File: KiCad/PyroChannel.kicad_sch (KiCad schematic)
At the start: 5 parts, among them Q1 IRLML0030

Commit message: very rough sketch layout
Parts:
- renumbered R2 to R10, R3 to R7, R4 to R8, R1 to R9
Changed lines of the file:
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@@
 		(dnp no)
 		(fields_autoplaced yes)
-		(property "Reference" "#PWR03"
+		(property "Reference" "#PWR040"
 			(at 157.48 107.95 0)
 			(effects
@@
 			(project ""
 				(path "/16f8cce7-467e-4342-b55a-00af81cd6f69/fc7ffde7-f19b-4eb6-b923-3f87c2b4142b"
-					(reference "#PWR03")
+					(reference "#PWR040")
 					(unit 1)
 				)
@@
 		(dnp no)
 		(fields_autoplaced yes)
-		(property "Reference" "#PWR02"
+		(property "Reference" "#PWR039"
 			(at 147.32 107.95 0)
 			(effects
@@
 			(project ""
 				(path "/16f8cce7-467e-4342-b55a-00af81cd6f69/fc7ffde7-f19b-4eb6-b923-3f87c2b4142b"
-					(reference "#PWR02")
+					(reference "#PWR039")
 					(unit 1)
 				)
@@
 		(dnp no)
 		(fields_autoplaced yes)
-		(property "Reference" "R1"
+		(property "Reference" "R9"
 			(at 160.02 81.2799 0)
 			(effects
@@
 			(project ""
 				(path "/16f8cce7-467e-4342-b55a-00af81cd6f69/fc7ffde7-f19b-4eb6-b923-3f87c2b4142b"
-					(reference "R1")
+					(reference "R9")
 					(unit 1)
 				)
@@
 		(dnp no)
 		(fields_autoplaced yes)
-		(property "Reference" "#PWR01"
+		(property "Reference" "#PWR038"
 			(at 138.43 115.57 0)
 			(effects
@@
 			(project ""
 				(path "/16f8cce7-467e-4342-b55a-00af81cd6f69/fc7ffde7-f19b-4eb6-b923-3f87c2b4142b"
-					(reference "#PWR01")
+					(reference "#PWR038")
 					(unit 1)
 				)
@@
 		(dnp no)
 		(fields_autoplaced yes)
-		(property "Reference" "R3"
+		(property "Reference" "R7"
 			(at 129.54 87.63 90)
 			(effects
@@
 			(project ""
 				(path "/16f8cce7-467e-4342-b55a-00af81cd6f69/fc7ffde7-f19b-4eb6-b923-3f87c2b4142b"
-					(reference "R3")
+					(reference "R7")
 					(unit 1)
 				)
@@
 		(dnp no)
 		(fields_autoplaced yes)
-		(property "Reference" "R4"
+		(property "Reference" "R8"
 			(at 140.97 104.1399 0)
 			(effects
@@
 			(project ""
 				(path "/16f8cce7-467e-4342-b55a-00af81cd6f69/fc7ffde7-f19b-4eb6-b923-3f87c2b4142b"
-					(reference "R4")
+					(reference "R8")
 					(unit 1)
 				)
@@
 		(dnp no)
 		(fields_autoplaced yes)
-		(property "Reference" "R2"
+		(property "Reference" "R10"
 			(at 160.02 95.2499 0)
 			(effects
@@
 			(project ""
 				(path "/16f8cce7-467e-4342-b55a-00af81cd6f69/fc7ffde7-f19b-4eb6-b923-3f87c2b4142b"
-					(reference "R2")
-					(unit 1)
-				)
+					(reference "R10")
+					(unit 1)
+				)

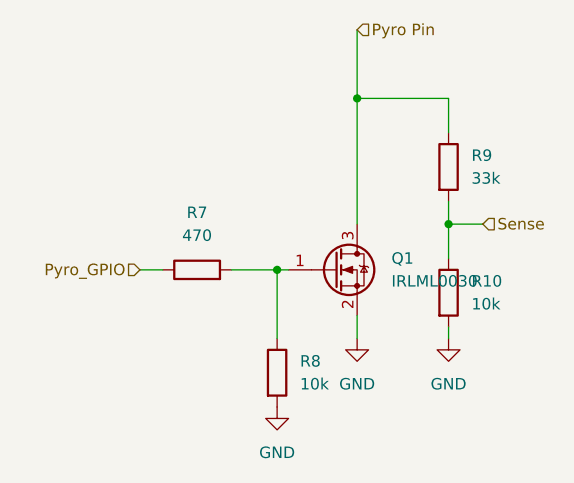
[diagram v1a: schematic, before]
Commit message: Added Pyrochannels
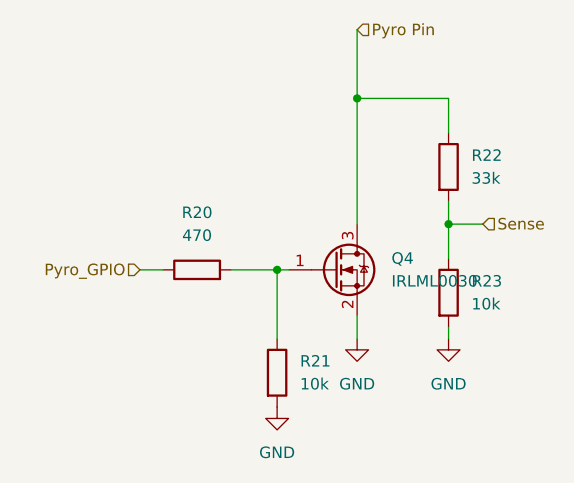
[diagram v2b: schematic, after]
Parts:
- renumbered Q1 to Q4, R7 to R20, R8 to R21, R9 to R22, R10 to R23
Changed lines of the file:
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@@
 		(dnp no)
 		(fields_autoplaced yes)
-		(property "Reference" "#PWR040"
+		(property "Reference" "#PWR072"
 			(at 157.48 107.95 0)
 			(effects
@@
 		)
 		(instances
-			(project ""
-				(path "/16f8cce7-467e-4342-b55a-00af81cd6f69/fc7ffde7-f19b-4eb6-b923-3f87c2b4142b"
-					(reference "#PWR040")
-					(unit 1)
-				)
-			)
-			(project ""
-				(path "/4b87987a-7eb1-4c92-aab7-f7fab4804919"
-					(reference "#PWR03")
+			(project "Senior Project"
+				(path "/16f8cce7-467e-4342-b55a-00af81cd6f69/4f56c78f-4532-4c9f-be6c-2bbf693c5fca"
+					(reference "#PWR072")
+					(unit 1)
+				)
+				(path "/16f8cce7-467e-4342-b55a-00af81cd6f69/528e247e-1625-48b4-9899-73b4b85367ce"
+					(reference "#PWR069")
+					(unit 1)
+				)
+				(path "/16f8cce7-467e-4342-b55a-00af81cd6f69/553e2c15-6dd9-455d-b91b-1c20c70d481b"
+					(reference "#PWR066")
 					(unit 1)
 				)
@@
 		(dnp no)
 		(fields_autoplaced yes)
-		(property "Reference" "#PWR039"
+		(property "Reference" "#PWR071"
 			(at 147.32 107.95 0)
 			(effects
@@
 		)
 		(instances
-			(project ""
-				(path "/16f8cce7-467e-4342-b55a-00af81cd6f69/fc7ffde7-f19b-4eb6-b923-3f87c2b4142b"
-					(reference "#PWR039")
-					(unit 1)
-				)
-			)
-			(project ""
-				(path "/4b87987a-7eb1-4c92-aab7-f7fab4804919"
-					(reference "#PWR02")
+			(project "Senior Project"
+				(path "/16f8cce7-467e-4342-b55a-00af81cd6f69/4f56c78f-4532-4c9f-be6c-2bbf693c5fca"
+					(reference "#PWR071")
+					(unit 1)
+				)
+				(path "/16f8cce7-467e-4342-b55a-00af81cd6f69/528e247e-1625-48b4-9899-73b4b85367ce"
+					(reference "#PWR068")
+					(unit 1)
+				)
+				(path "/16f8cce7-467e-4342-b55a-00af81cd6f69/553e2c15-6dd9-455d-b91b-1c20c70d481b"
+					(reference "#PWR057")
 					(unit 1)
 				)
@@
 		(dnp no)
 		(fields_autoplaced yes)
-		(property "Reference" "R9"
+		(property "Reference" "R22"
 			(at 160.02 81.2799 0)
 			(effects
@@
 		)
 		(instances
-			(project ""
-				(path "/16f8cce7-467e-4342-b55a-00af81cd6f69/fc7ffde7-f19b-4eb6-b923-3f87c2b4142b"
-					(reference "R9")
-					(unit 1)
-				)
-			)
-			(project ""
-				(path "/4b87987a-7eb1-4c92-aab7-f7fab4804919"
-					(reference "R1")
+			(project "Senior Project"
+				(path "/16f8cce7-467e-4342-b55a-00af81cd6f69/4f56c78f-4532-4c9f-be6c-2bbf693c5fca"
+					(reference "R22")
+					(unit 1)
+				)
+				(path "/16f8cce7-467e-4342-b55a-00af81cd6f69/528e247e-1625-48b4-9899-73b4b85367ce"
+					(reference "R18")
+					(unit 1)
+				)
+				(path "/16f8cce7-467e-4342-b55a-00af81cd6f69/553e2c15-6dd9-455d-b91b-1c20c70d481b"
+					(reference "R14")
 					(unit 1)
 				)
@@
 		(dnp no)
 		(fields_autoplaced yes)
-		(property "Reference" "#PWR038"
+		(property "Reference" "#PWR070"
 			(at 138.43 115.57 0)
 			(effects
@@
 		)
 		(instances
-			(project ""
-				(path "/16f8cce7-467e-4342-b55a-00af81cd6f69/fc7ffde7-f19b-4eb6-b923-3f87c2b4142b"
-					(reference "#PWR038")
-					(unit 1)
-				)
-			)
-			(project ""
-				(path "/4b87987a-7eb1-4c92-aab7-f7fab4804919"
-					(reference "#PWR01")
+			(project "Senior Project"
+				(path "/16f8cce7-467e-4342-b55a-00af81cd6f69/4f56c78f-4532-4c9f-be6c-2bbf693c5fca"
+					(reference "#PWR070")
+					(unit 1)
+				)
+				(path "/16f8cce7-467e-4342-b55a-00af81cd6f69/528e247e-1625-48b4-9899-73b4b85367ce"
+					(reference "#PWR067")
+					(unit 1)
+				)
+				(path "/16f8cce7-467e-4342-b55a-00af81cd6f69/553e2c15-6dd9-455d-b91b-1c20c70d481b"
+					(reference "#PWR056")
 					(unit 1)
 				)
@@
 		(dnp no)
 		(fields_autoplaced yes)
-		(property "Reference" "R7"
+		(property "Reference" "R20"
 			(at 129.54 87.63 90)
 			(effects
@@
 		)
 		(instances
-			(project ""
-				(path "/16f8cce7-467e-4342-b55a-00af81cd6f69/fc7ffde7-f19b-4eb6-b923-3f87c2b4142b"
-					(reference "R7")
-					(unit 1)
-				)
-			)
-			(project ""
-				(path "/4b87987a-7eb1-4c92-aab7-f7fab4804919"
-					(reference "R3")
+			(project "Senior Project"
+				(path "/16f8cce7-467e-4342-b55a-00af81cd6f69/4f56c78f-4532-4c9f-be6c-2bbf693c5fca"
+					(reference "R20")
+					(unit 1)
+				)
+				(path "/16f8cce7-467e-4342-b55a-00af81cd6f69/528e247e-1625-48b4-9899-73b4b85367ce"
+					(reference "R16")
+					(unit 1)
+				)
+				(path "/16f8cce7-467e-4342-b55a-00af81cd6f69/553e2c15-6dd9-455d-b91b-1c20c70d481b"
+					(reference "R12")
 					(unit 1)
 				)
@@
 		(dnp no)
 		(fields_autoplaced yes)
-		(property "Reference" "Q1"
+		(property "Reference" "Q4"
 			(at 151.13 92.7099 0)
 			(effects
@@
 		)
 		(instances
-			(project ""
-				(path "/16f8cce7-467e-4342-b55a-00af81cd6f69/fc7ffde7-f19b-4eb6-b923-3f87c2b4142b"
-					(reference "Q1")
-					(unit 1)
-				)
-			)
-			(project ""
-				(path "/4b87987a-7eb1-4c92-aab7-f7fab4804919"
-					(reference "Q1")
+			(project "Senior Project"
+				(path "/16f8cce7-467e-4342-b55a-00af81cd6f69/4f56c78f-4532-4c9f-be6c-2bbf693c5fca"
+					(reference "Q4")
+					(unit 1)
+				)
+				(path "/16f8cce7-467e-4342-b55a-00af81cd6f69/528e247e-1625-48b4-9899-73b4b85367ce"
+					(reference "Q3")
+					(unit 1)
+				)
+				(path "/16f8cce7-467e-4342-b55a-00af81cd6f69/553e2c15-6dd9-455d-b91b-1c20c70d481b"
+					(reference "Q2")
 					(unit 1)
 				)
@@
 		(dnp no)
 		(fields_autoplaced yes)
-		(property "Reference" "R8"
+		(property "Reference" "R21"
 			(at 140.97 104.1399 0)
 			(effects
@@
 		)
 		(instances
-			(project ""
-				(path "/16f8cce7-467e-4342-b55a-00af81cd6f69/fc7ffde7-f19b-4eb6-b923-3f87c2b4142b"
-					(reference "R8")
-					(unit 1)
-				)
-			)
-			(project ""
-				(path "/4b87987a-7eb1-4c92-aab7-f7fab4804919"
-					(reference "R4")
+			(project "Senior Project"
+				(path "/16f8cce7-467e-4342-b55a-00af81cd6f69/4f56c78f-4532-4c9f-be6c-2bbf693c5fca"
+					(reference "R21")
+					(unit 1)
+				)
+				(path "/16f8cce7-467e-4342-b55a-00af81cd6f69/528e247e-1625-48b4-9899-73b4b85367ce"
+					(reference "R17")
+					(unit 1)
+				)
+				(path "/16f8cce7-467e-4342-b55a-00af81cd6f69/553e2c15-6dd9-455d-b91b-1c20c70d481b"
+					(reference "R13")
 					(unit 1)
 				)
@@
 		(dnp no)
 		(fields_autoplaced yes)
-		(property "Reference" "R10"
+		(property "Reference" "R23"
 			(at 160.02 95.2499 0)
 			(effects
@@
 		)
 		(instances
-			(project ""
-				(path "/16f8cce7-467e-4342-b55a-00af81cd6f69/fc7ffde7-f19b-4eb6-b923-3f87c2b4142b"
-					(reference "R10")
-					(unit 1)
-				)
-			)
-			(project ""
-				(path "/4b87987a-7eb1-4c92-aab7-f7fab4804919"
-					(reference "R2")
-					(unit 1)
-				)
+			(project "Senior Project"
+				(path "/16f8cce7-467e-4342-b55a-00af81cd6f69/4f56c78f-4532-4c9f-be6c-2bbf693c5fca"
+					(reference "R23")
+					(unit 1)
+				)
+				(path "/16f8cce7-467e-4342-b55a-00af81cd6f69/528e247e-1625-48b4-9899-73b4b85367ce"
+					(reference "R19")
+					(unit 1)
+				)
+				(path "/16f8cce7-467e-4342-b55a-00af81cd6f69/553e2c15-6dd9-455d-b91b-1c20c70d481b"
+					(reference "R15")
+					(unit 1)
+				)

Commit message: Layout started
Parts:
- renumbered Q4 to Q3, R20 to R16, R21 to R17, R22 to R18, R23 to R19
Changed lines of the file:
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@@
 		(dnp no)
 		(fields_autoplaced yes)
-		(property "Reference" "#PWR072"
+		(property "Reference" "#PWR069"
 			(at 157.48 107.95 0)
 			(effects
@@
 		(instances
 			(project "Senior Project"
-				(path "/16f8cce7-467e-4342-b55a-00af81cd6f69/4f56c78f-4532-4c9f-be6c-2bbf693c5fca"
+				(path "/16f8cce7-467e-4342-b55a-00af81cd6f69/553e2c15-6dd9-455d-b91b-1c20c70d481b"
+					(reference "#PWR066")
+					(unit 1)
+				)
+				(path "/16f8cce7-467e-4342-b55a-00af81cd6f69/60268ff6-e480-4c50-9139-8340585ef982"
+					(reference "#PWR069")
+					(unit 1)
+				)
+				(path "/16f8cce7-467e-4342-b55a-00af81cd6f69/93da445a-87ee-42db-a7a9-6194d5b9218b"
 					(reference "#PWR072")
-					(unit 1)
-				)
-				(path "/16f8cce7-467e-4342-b55a-00af81cd6f69/528e247e-1625-48b4-9899-73b4b85367ce"
-					(reference "#PWR069")
-					(unit 1)
-				)
-				(path "/16f8cce7-467e-4342-b55a-00af81cd6f69/553e2c15-6dd9-455d-b91b-1c20c70d481b"
-					(reference "#PWR066")
 					(unit 1)
 				)
@@
 		(dnp no)
 		(fields_autoplaced yes)
-		(property "Reference" "#PWR071"
+		(property "Reference" "#PWR068"
 			(at 147.32 107.95 0)
 			(effects
@@
 		(instances
 			(project "Senior Project"
-				(path "/16f8cce7-467e-4342-b55a-00af81cd6f69/4f56c78f-4532-4c9f-be6c-2bbf693c5fca"
+				(path "/16f8cce7-467e-4342-b55a-00af81cd6f69/553e2c15-6dd9-455d-b91b-1c20c70d481b"
+					(reference "#PWR057")
+					(unit 1)
+				)
+				(path "/16f8cce7-467e-4342-b55a-00af81cd6f69/60268ff6-e480-4c50-9139-8340585ef982"
+					(reference "#PWR068")
+					(unit 1)
+				)
+				(path "/16f8cce7-467e-4342-b55a-00af81cd6f69/93da445a-87ee-42db-a7a9-6194d5b9218b"
 					(reference "#PWR071")
-					(unit 1)
-				)
-				(path "/16f8cce7-467e-4342-b55a-00af81cd6f69/528e247e-1625-48b4-9899-73b4b85367ce"
-					(reference "#PWR068")
-					(unit 1)
-				)
-				(path "/16f8cce7-467e-4342-b55a-00af81cd6f69/553e2c15-6dd9-455d-b91b-1c20c70d481b"
-					(reference "#PWR057")
 					(unit 1)
 				)
@@
 		(dnp no)
 		(fields_autoplaced yes)
-		(property "Reference" "R22"
+		(property "Reference" "R18"
 			(at 160.02 81.2799 0)
 			(effects
@@
 		(instances
 			(project "Senior Project"
-				(path "/16f8cce7-467e-4342-b55a-00af81cd6f69/4f56c78f-4532-4c9f-be6c-2bbf693c5fca"
+				(path "/16f8cce7-467e-4342-b55a-00af81cd6f69/553e2c15-6dd9-455d-b91b-1c20c70d481b"
+					(reference "R14")
+					(unit 1)
+				)
+				(path "/16f8cce7-467e-4342-b55a-00af81cd6f69/60268ff6-e480-4c50-9139-8340585ef982"
+					(reference "R18")
+					(unit 1)
+				)
+				(path "/16f8cce7-467e-4342-b55a-00af81cd6f69/93da445a-87ee-42db-a7a9-6194d5b9218b"
 					(reference "R22")
-					(unit 1)
-				)
-				(path "/16f8cce7-467e-4342-b55a-00af81cd6f69/528e247e-1625-48b4-9899-73b4b85367ce"
-					(reference "R18")
-					(unit 1)
-				)
-				(path "/16f8cce7-467e-4342-b55a-00af81cd6f69/553e2c15-6dd9-455d-b91b-1c20c70d481b"
-					(reference "R14")
 					(unit 1)
 				)
@@
 		(dnp no)
 		(fields_autoplaced yes)
-		(property "Reference" "#PWR070"
+		(property "Reference" "#PWR067"
 			(at 138.43 115.57 0)
 			(effects
@@
 		(instances
 			(project "Senior Project"
-				(path "/16f8cce7-467e-4342-b55a-00af81cd6f69/4f56c78f-4532-4c9f-be6c-2bbf693c5fca"
+				(path "/16f8cce7-467e-4342-b55a-00af81cd6f69/553e2c15-6dd9-455d-b91b-1c20c70d481b"
+					(reference "#PWR056")
+					(unit 1)
+				)
+				(path "/16f8cce7-467e-4342-b55a-00af81cd6f69/60268ff6-e480-4c50-9139-8340585ef982"
+					(reference "#PWR067")
+					(unit 1)
+				)
+				(path "/16f8cce7-467e-4342-b55a-00af81cd6f69/93da445a-87ee-42db-a7a9-6194d5b9218b"
 					(reference "#PWR070")
-					(unit 1)
-				)
-				(path "/16f8cce7-467e-4342-b55a-00af81cd6f69/528e247e-1625-48b4-9899-73b4b85367ce"
-					(reference "#PWR067")
-					(unit 1)
-				)
-				(path "/16f8cce7-467e-4342-b55a-00af81cd6f69/553e2c15-6dd9-455d-b91b-1c20c70d481b"
-					(reference "#PWR056")
 					(unit 1)
 				)
@@
 		(dnp no)
 		(fields_autoplaced yes)
-		(property "Reference" "R20"
+		(property "Reference" "R16"
 			(at 129.54 87.63 90)
 			(effects
@@
 		(instances
 			(project "Senior Project"
-				(path "/16f8cce7-467e-4342-b55a-00af81cd6f69/4f56c78f-4532-4c9f-be6c-2bbf693c5fca"
+				(path "/16f8cce7-467e-4342-b55a-00af81cd6f69/553e2c15-6dd9-455d-b91b-1c20c70d481b"
+					(reference "R12")
+					(unit 1)
+				)
+				(path "/16f8cce7-467e-4342-b55a-00af81cd6f69/60268ff6-e480-4c50-9139-8340585ef982"
+					(reference "R16")
+					(unit 1)
+				)
+				(path "/16f8cce7-467e-4342-b55a-00af81cd6f69/93da445a-87ee-42db-a7a9-6194d5b9218b"
 					(reference "R20")
-					(unit 1)
-				)
-				(path "/16f8cce7-467e-4342-b55a-00af81cd6f69/528e247e-1625-48b4-9899-73b4b85367ce"
-					(reference "R16")
-					(unit 1)
-				)
-				(path "/16f8cce7-467e-4342-b55a-00af81cd6f69/553e2c15-6dd9-455d-b91b-1c20c70d481b"
-					(reference "R12")
 					(unit 1)
 				)
@@
 		(dnp no)
 		(fields_autoplaced yes)
-		(property "Reference" "Q4"
+		(property "Reference" "Q3"
 			(at 151.13 92.7099 0)
 			(effects
@@
 		(instances
 			(project "Senior Project"
-				(path "/16f8cce7-467e-4342-b55a-00af81cd6f69/4f56c78f-4532-4c9f-be6c-2bbf693c5fca"
+				(path "/16f8cce7-467e-4342-b55a-00af81cd6f69/553e2c15-6dd9-455d-b91b-1c20c70d481b"
+					(reference "Q2")
+					(unit 1)
+				)
+				(path "/16f8cce7-467e-4342-b55a-00af81cd6f69/60268ff6-e480-4c50-9139-8340585ef982"
+					(reference "Q3")
+					(unit 1)
+				)
+				(path "/16f8cce7-467e-4342-b55a-00af81cd6f69/93da445a-87ee-42db-a7a9-6194d5b9218b"
 					(reference "Q4")
-					(unit 1)
-				)
-				(path "/16f8cce7-467e-4342-b55a-00af81cd6f69/528e247e-1625-48b4-9899-73b4b85367ce"
-					(reference "Q3")
-					(unit 1)
-				)
-				(path "/16f8cce7-467e-4342-b55a-00af81cd6f69/553e2c15-6dd9-455d-b91b-1c20c70d481b"
-					(reference "Q2")
 					(unit 1)
 				)
@@
 		(dnp no)
 		(fields_autoplaced yes)
-		(property "Reference" "R21"
+		(property "Reference" "R17"
 			(at 140.97 104.1399 0)
 			(effects
@@
 		(instances
 			(project "Senior Project"
-				(path "/16f8cce7-467e-4342-b55a-00af81cd6f69/4f56c78f-4532-4c9f-be6c-2bbf693c5fca"
+				(path "/16f8cce7-467e-4342-b55a-00af81cd6f69/553e2c15-6dd9-455d-b91b-1c20c70d481b"
+					(reference "R13")
+					(unit 1)
+				)
+				(path "/16f8cce7-467e-4342-b55a-00af81cd6f69/60268ff6-e480-4c50-9139-8340585ef982"
+					(reference "R17")
+					(unit 1)
+				)
+				(path "/16f8cce7-467e-4342-b55a-00af81cd6f69/93da445a-87ee-42db-a7a9-6194d5b9218b"
 					(reference "R21")
-					(unit 1)
-				)
-				(path "/16f8cce7-467e-4342-b55a-00af81cd6f69/528e247e-1625-48b4-9899-73b4b85367ce"
-					(reference "R17")
-					(unit 1)
-				)
-				(path "/16f8cce7-467e-4342-b55a-00af81cd6f69/553e2c15-6dd9-455d-b91b-1c20c70d481b"
-					(reference "R13")
 					(unit 1)
 				)
@@
 		(dnp no)
 		(fields_autoplaced yes)
-		(property "Reference" "R23"
+		(property "Reference" "R19"
 			(at 160.02 95.2499 0)
 			(effects
@@
 		(instances
 			(project "Senior Project"
-				(path "/16f8cce7-467e-4342-b55a-00af81cd6f69/4f56c78f-4532-4c9f-be6c-2bbf693c5fca"
+				(path "/16f8cce7-467e-4342-b55a-00af81cd6f69/553e2c15-6dd9-455d-b91b-1c20c70d481b"
+					(reference "R15")
+					(unit 1)
+				)
+				(path "/16f8cce7-467e-4342-b55a-00af81cd6f69/60268ff6-e480-4c50-9139-8340585ef982"
+					(reference "R19")
+					(unit 1)
+				)
+				(path "/16f8cce7-467e-4342-b55a-00af81cd6f69/93da445a-87ee-42db-a7a9-6194d5b9218b"
 					(reference "R23")
 					(unit 1)
 				)
-				(path "/16f8cce7-467e-4342-b55a-00af81cd6f69/528e247e-1625-48b4-9899-73b4b85367ce"
-					(reference "R19")
-					(unit 1)
-				)
-				(path "/16f8cce7-467e-4342-b55a-00af81cd6f69/553e2c15-6dd9-455d-b91b-1c20c70d481b"
-					(reference "R15")
-					(unit 1)
-				)

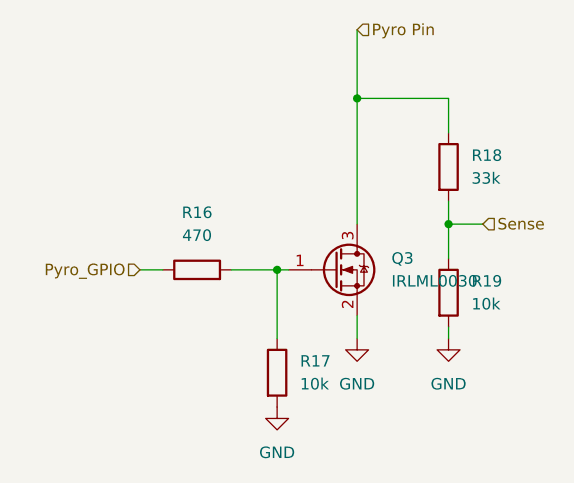
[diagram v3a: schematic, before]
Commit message: tighten up layout, swap out USB connector
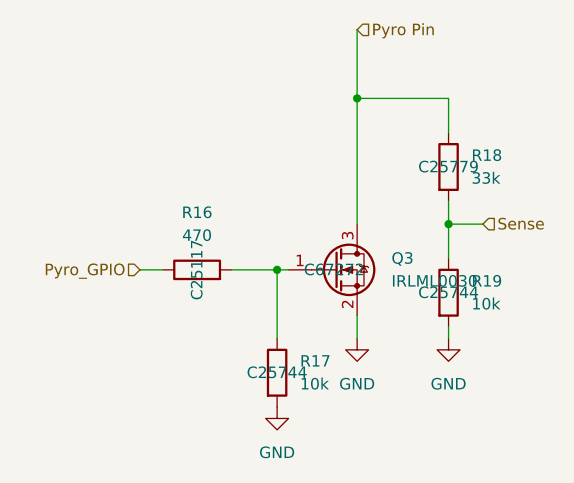
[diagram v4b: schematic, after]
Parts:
- Q3: LCSC (none) -> C67272
- R16: LCSC (none) -> C25117
- R17, R19: LCSC (none) -> C25744
- R18: LCSC (none) -> C25779
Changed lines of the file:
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@@
+			)
+		)
+		(property "LCSC" "C25779"
+			(at 157.48 82.55 0)
+			(effects
+				(font
+					(size 1.27 1.27)
+				)
 			)
 		)
@@
 			)
 		)
+		(property "LCSC" "C25117"
+			(at 129.54 93.98 0)
+			(effects
+				(font
+					(size 1.27 1.27)
+				)
+			)
+		)
 		(pin "2"
 		)
@@
 			)
 		)
+		(property "LCSC" "C67272"
+			(at 144.78 93.98 0)
+			(effects
+				(font
+					(size 1.27 1.27)
+				)
+			)
+		)
 		(pin "1"
 		)
@@
 			)
 		)
+		(property "LCSC" "C25744"
+			(at 138.43 105.41 0)
+			(effects
+				(font
+					(size 1.27 1.27)
+				)
+			)
+		)
 		(pin "2"
 		)
@@
 			)
 		)
+		(property "LCSC" "C25744"
+			(at 157.48 96.52 0)
+			(effects
+				(font
+					(size 1.27 1.27)
+				)
+			)
+		)
